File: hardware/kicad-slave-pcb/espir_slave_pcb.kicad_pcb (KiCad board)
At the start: 2 copper layers, 53.5 x 47 mm, 38 parts, among them Q2 AO3400A, Q4 AO3401A, SW1 RESET, SW2 BOOT, SW3 SS12D07VG6, U2 IR333C, U3 IR333C, U5 ESP32-C6-MINI-1, U6 AP2112K-3.3, U7 LiPo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

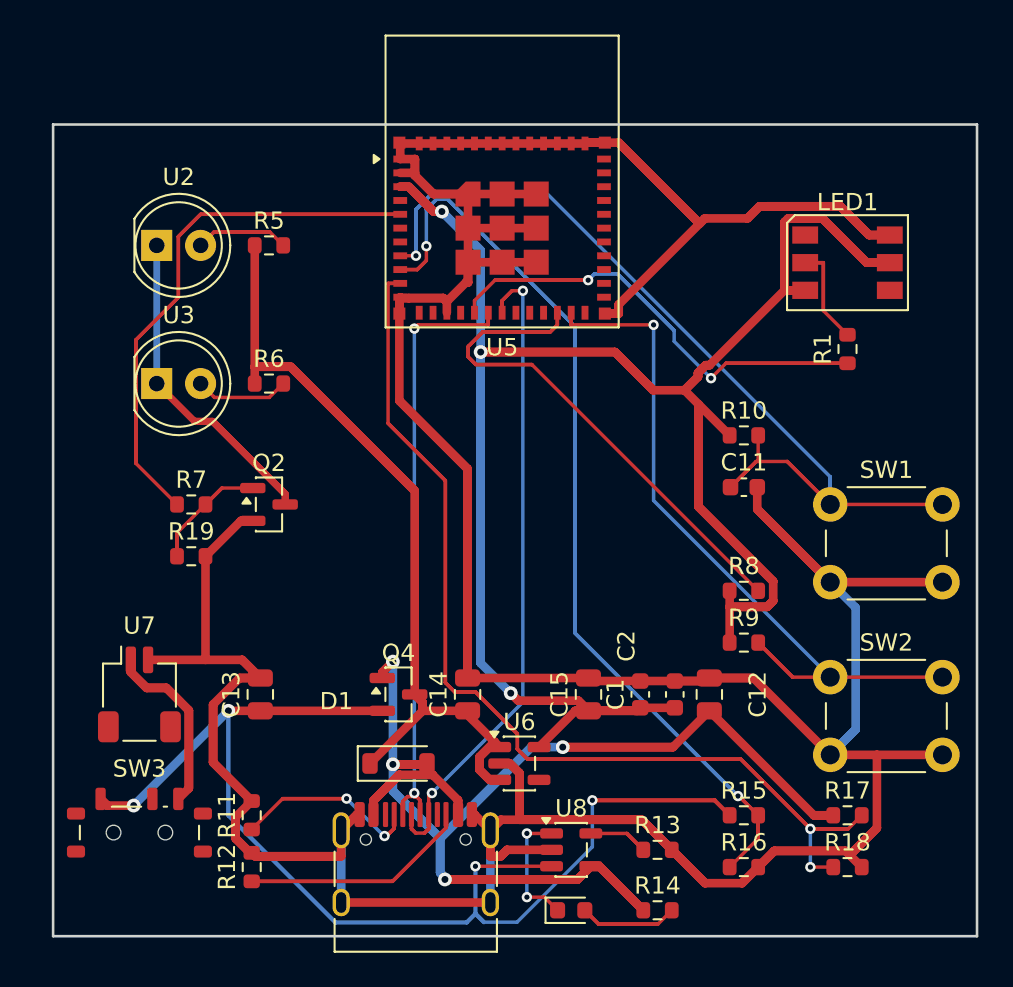
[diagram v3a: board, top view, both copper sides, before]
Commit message: hardware: convert slave PCB to 4-layer, wide VBAT, GND planes
Per request — minimal cost delta, don't sacrifice stability:
- 4 copper layers (F/In1/In2/B) via place_and_outline; GND pours on all four
  layers + collision-checked stitching-via grid (pour_gnd.py) → inner ground
  reference planes.
- The extra routing room lets every Power-class rail, including VBAT, route at
  0.5 mm (dropped the 2-layer VBAT 0.2 mm compromise; .kicad_dru back to 0.5).
- Fully routed 114/114 (310 tracks, 43 vias). LDO EN (tied to VSYS, boxed by
  U6's VIN/GND pins) jumpered VIN→EN on B.Cu under the GND pin.
- Grew board to 54 mm wide so the edge buttons clear the edge without colliding
  with the strap resistors; re-centred on A4.
- Silkscreen: collision-aware designator placement (fix_silk.py), hide refs with
  no clear spot.

DRC: 0 electrical violations (0 unconnected/track-width/clearance/edge/shorts).
Remaining 4 silk_edge_clearance (antenna/USB-C outlines overhang edges, by design)
+ 1 lib_footprint_mismatch (U5 vs latest library, same 61 pads, benign).
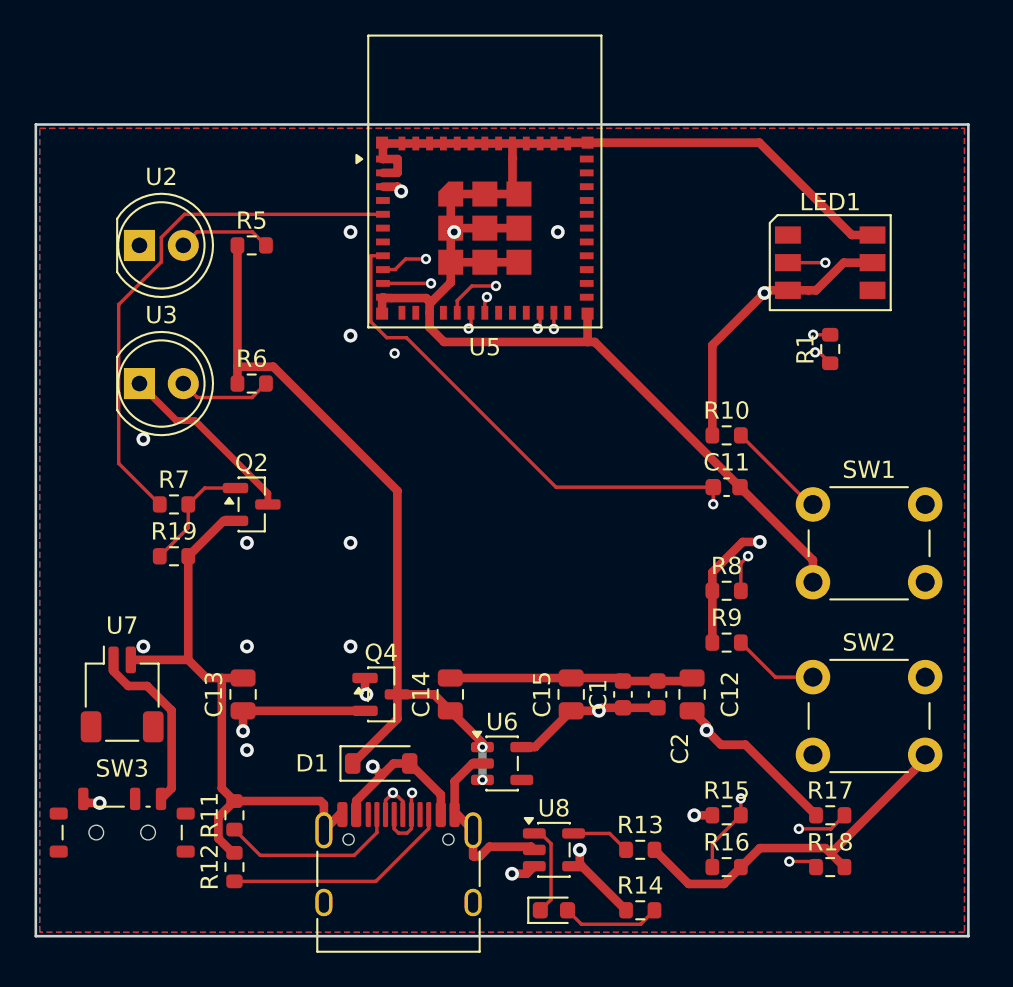
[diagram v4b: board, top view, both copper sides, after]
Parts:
- moved C1 1.00 mm to (155.5, 114.5)
- moved C11 1.00 mm to (161.5, 102.5)
- moved C12 1.00 mm to (159.5, 114.5)
- moved C13 1.00 mm to (133.5, 114.5)
- moved C14 1.00 mm to (145.5, 114.5)
- moved C15 1.00 mm to (152.5, 114.5)
- moved C2 1.00 mm to (157.5, 114.5)
- moved D1 1.00 mm to (141.5, 118.5)
- moved LED1 1.00 mm to (167.5, 89.5)
- moved LED2 1.00 mm to (151.5, 127.0)
- moved Q2 1.00 mm to (134.0, 103.5)
- moved Q4 1.00 mm to (141.5, 114.5)
- moved R1 1.00 mm to (167.5, 94.5)
- moved R10 1.00 mm to (161.5, 99.5)
- moved R11 1.00 mm to (133.0, 121.5)
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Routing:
- net GND: track 351.8 -> 203.6 mm, vias 0 -> 11
- net V3V3: track 171.0 -> 86.2 mm, vias 3 -> 4
- net BATT_SENSE: track 100.6 -> 46.2 mm
- net V5: track 106.3 -> 53.7 mm
- net VBUS_SENSE: track 101.6 -> 51.6 mm, vias 2 -> 3
- net IR1: track 58.4 -> 30.9 mm
- net EN: track 69.7 -> 47.4 mm
- net WS_GPIO: track 45.1 -> 24.5 mm
- net STRAP8: track 40.2 -> 22.9 mm, vias 0 -> 2
- net VSYS: track 62.5 -> 45.3 mm, vias 0 -> 2
- net VBAT: track 69.4 -> 52.8 mm
- net N$2: track 25.8 -> 13.3 mm
- net VCELL: track 19.9 -> 10.3 mm
- net IRD: track 26.3 -> 18.7 mm
- net BOOT: track 45.1 -> 38.9 mm
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- added copper zone on B.Cu, net GND
- added copper zone on F.Cu, net GND
- added copper zone on In1.Cu, net GND
- added copper zone on In2.Cu, net GND
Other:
- board size 53.5 x 47 mm -> 54 x 47 mm
- copper layers 2 -> 4

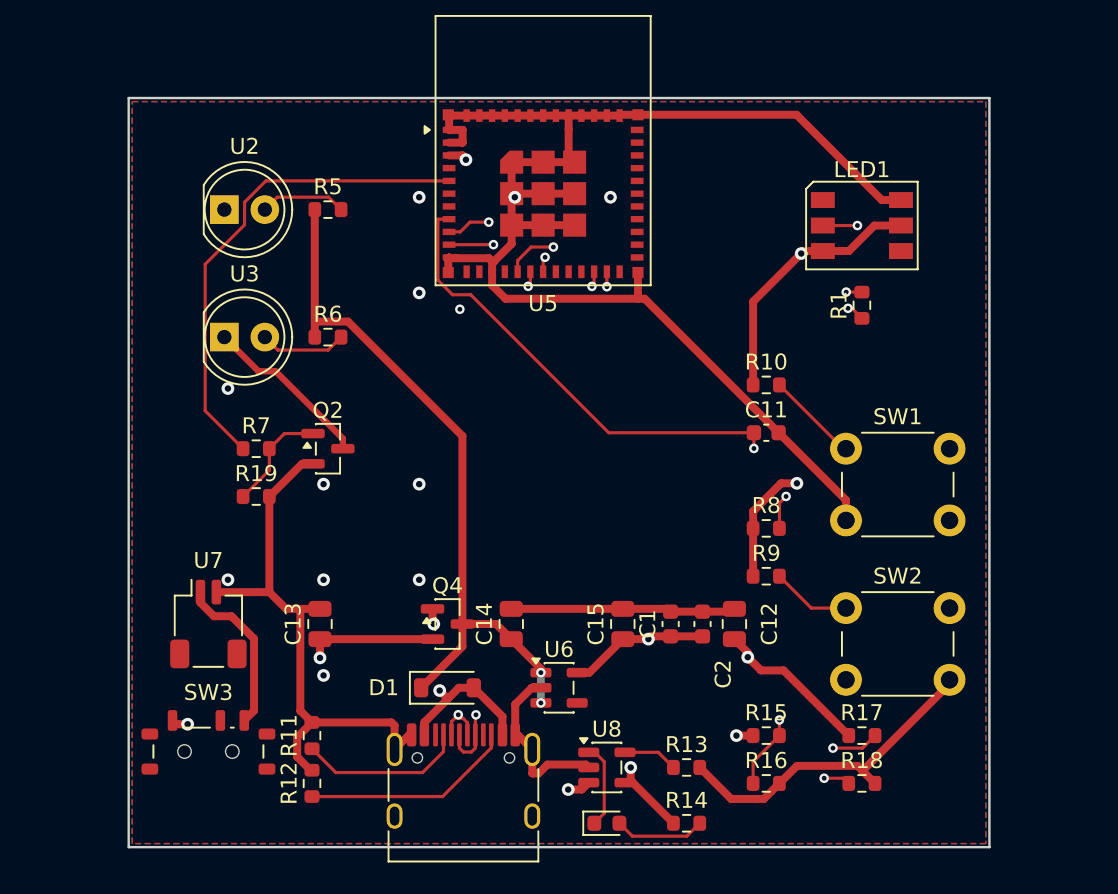
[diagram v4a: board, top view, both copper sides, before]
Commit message: hardware: round corners + 4x M3 mounting holes (expand board on X)
mounting_and_round.py (runs on the routed board — no re-route needed):
- expand the board on X to 66mm (symmetric, stays centred) so the packed
  components get clear left/right margins;
- round all four corners (r=3mm);
- add 4x M3 mounting holes (3.2mm Edge.Cuts cutouts) in the new margins, clear
  of every component — the GND pour isolates them with a ring.

pour_gnd.py: re-pour to the new outline; do all collection reads (tracks, pads)
before any writes (a SetLocalZoneConnection mid-iteration corrupts SWIG so a
later GetTracks returns a raw object); use SHAPE_LINE_CHAIN+AddPolygon for the
zone outline; treat existing vias as stitching obstacles (no hole_to_hole).

DRC: 0 unconnected, 0 electrical violations; 4 benign silk_edge + 1 benign
lib_footprint_mismatch.
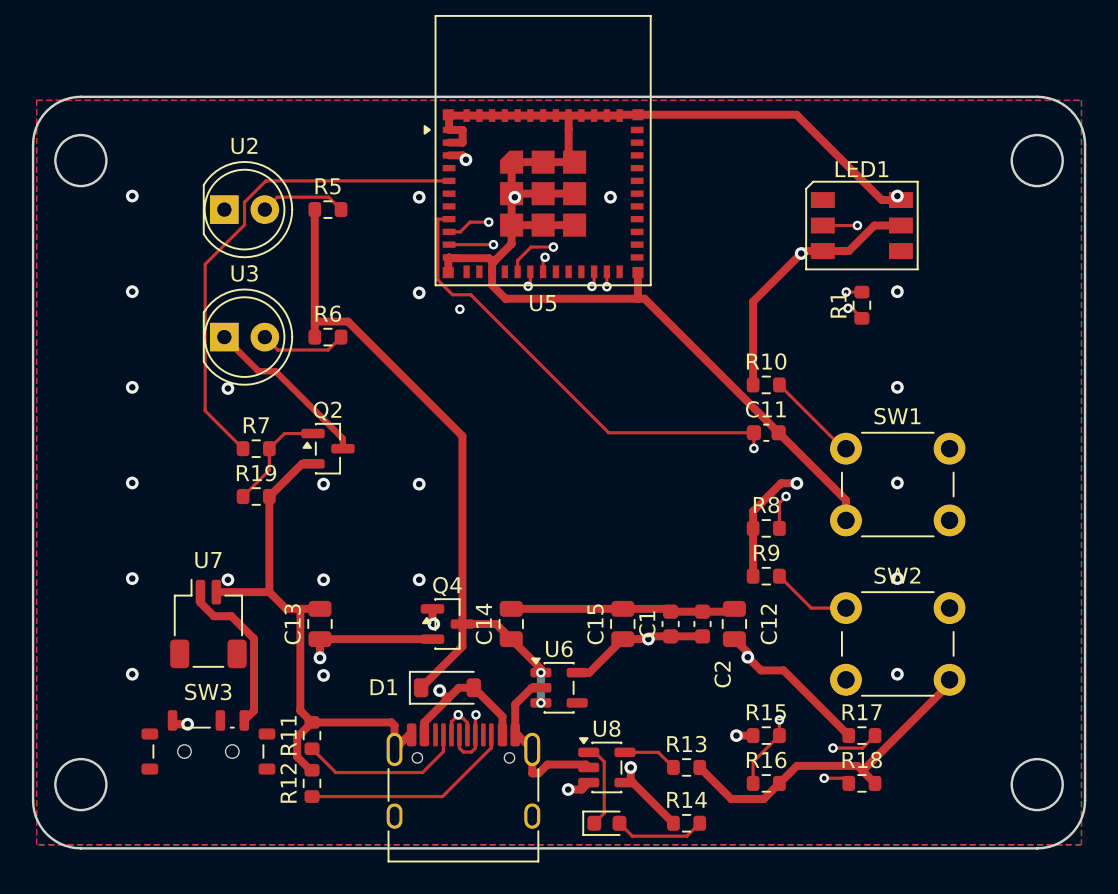
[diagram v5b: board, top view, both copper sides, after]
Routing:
- net GND: vias 11 -> 23
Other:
- board size 54 x 47 mm -> 66 x 47.1 mm

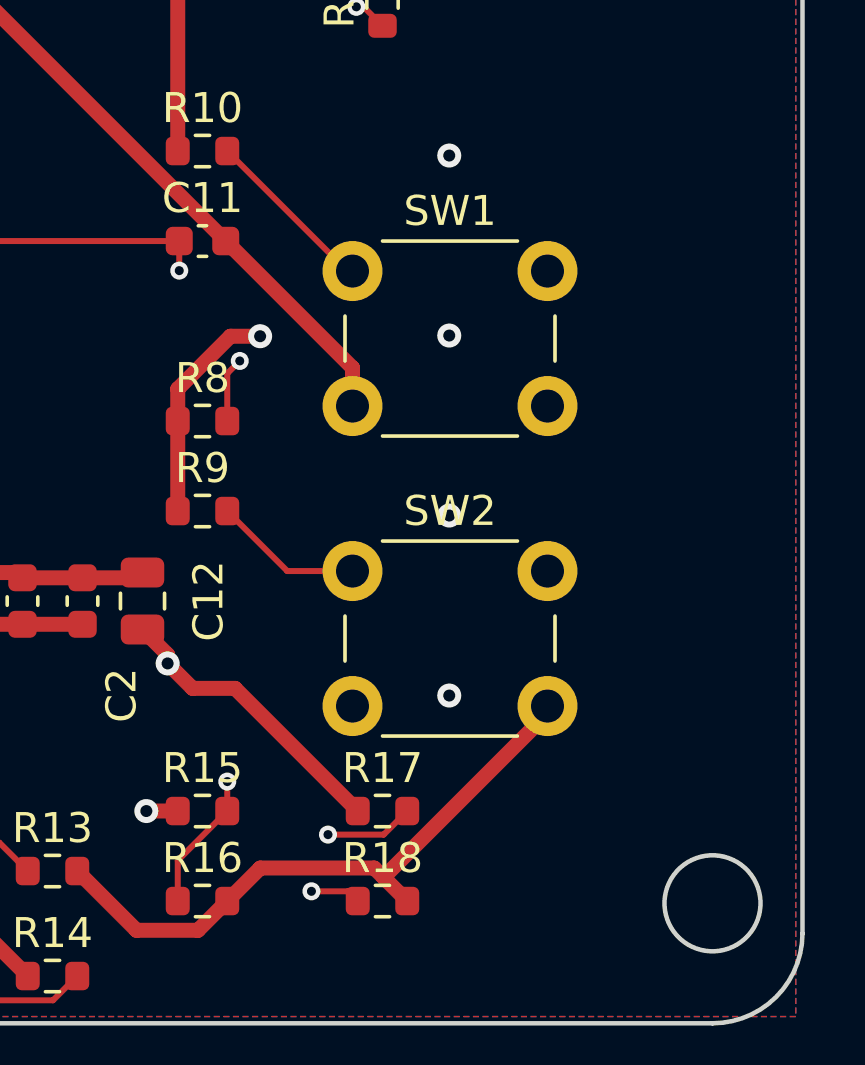
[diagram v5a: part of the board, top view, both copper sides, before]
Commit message: hardware: change RESET/BOOT buttons from THT 6mm to SMD tactile (KMR2)
Swap SW1/SW2 from Button_Switch_THT:SW_PUSH_6mm to
Button_Switch_SMD:SW_Push_1P1T_NO_CK_KMR2, in both the SKiDL source and the
routed board (swap_smd_button.py, run per-button in its own process to dodge
pcbnew SWIG state corruption):
- assign the new pads' nets AFTER Add (Add clears nets set beforehand);
- bridge the EN/BOOT signal once per old pad position to the nearest new pad;
- add a via at each old (through-hole) pad position so the inner/bottom-layer
  tracks that connected through the THT hole stay on-net;
- drop the dangling GND stubs — the 4-layer GND pour reconnects the new GND pads.

DRC: 0 unconnected, 0 electrical violations (only the 4 benign edge-silk + 1
benign lib_footprint_mismatch). 3D-verified the two SMD buttons.
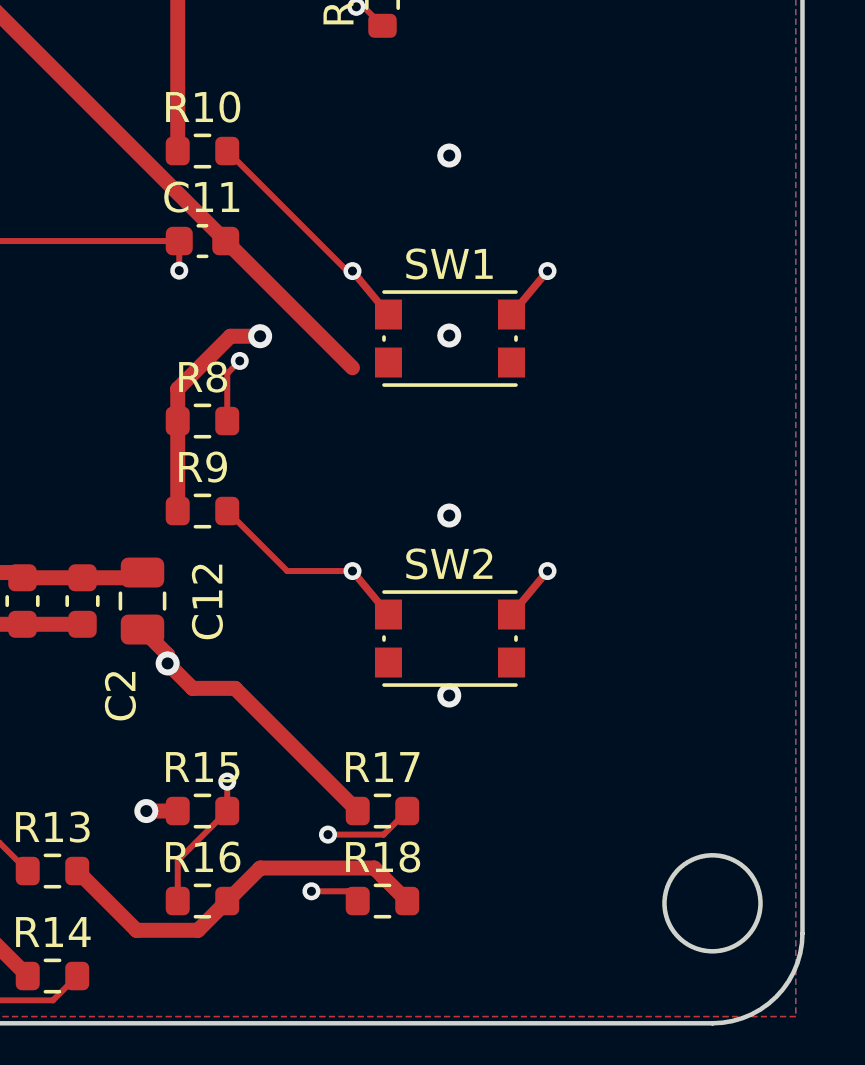
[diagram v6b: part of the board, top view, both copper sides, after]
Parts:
- SW1, SW2: footprint Button_Switch_THT:SW_PUSH_6mm -> SW_Push_1P1T_NO_CK_KMR2
- moved SW1 3.95 mm to (169.8, 105.8)
- moved SW2 3.95 mm to (169.8, 115.8)
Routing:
- net GND: track 203.6 -> 181.4 mm
- net EN: track 47.4 -> 51.2 mm, vias 1 -> 3
- net BOOT: track 38.9 -> 42.7 mm, vias 1 -> 3

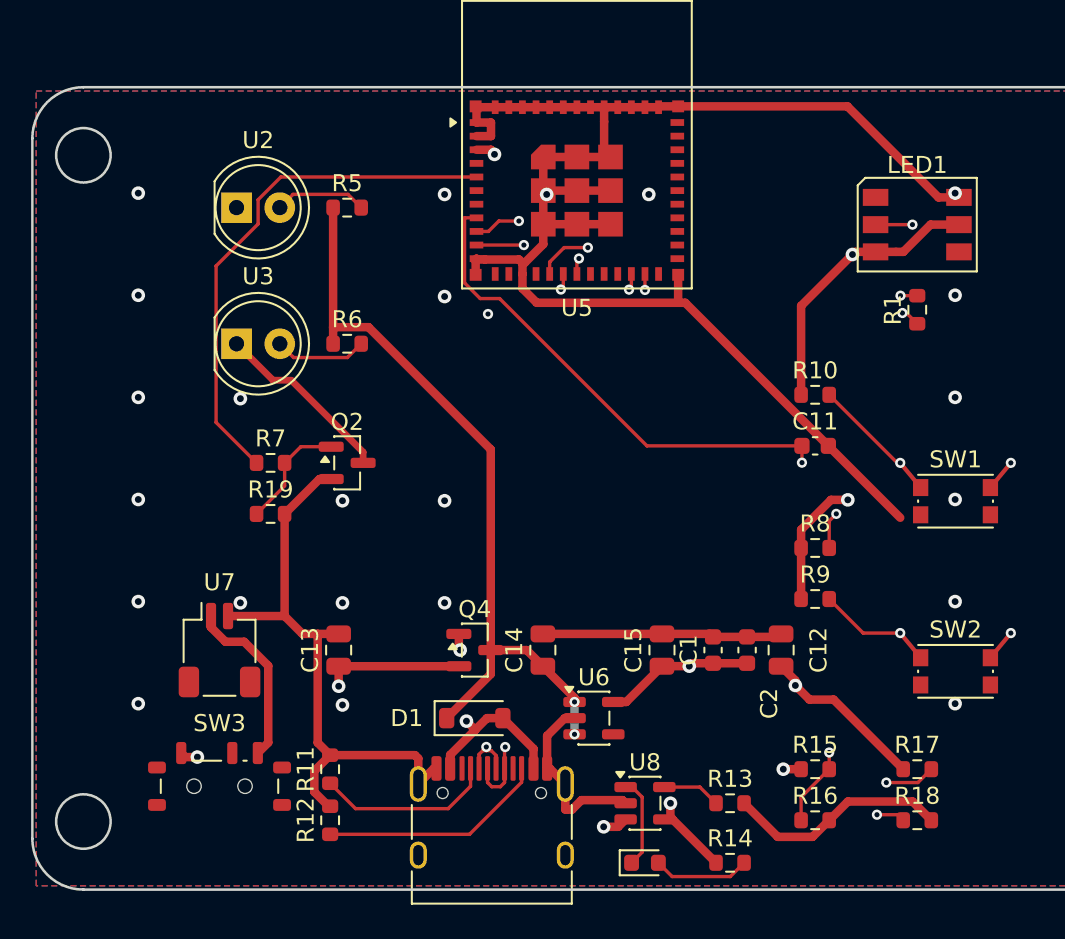
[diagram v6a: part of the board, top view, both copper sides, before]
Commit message: hardware: re-solve routing after U7 (JST battery connector) move
U7 was moved + rotated -90° in the GUI, which broke local routing:
- VCELL (U7.1 -> SW3.3) left dangling in two pieces -> cleared the fragments
  and re-routed it on F.Cu (right, then down, clear of U7's own GND pad), 0.5mm
  Power class;
- U7's mounting pads landed on two GND stitch vias (short + hole-clearance +
  mask-bridge) -> removed those two vias (the pour still grounds the area);
- trimmed a stray dangling V3V3 stub.
Re-poured all four GND layers.

DRC: 0 unconnected, 0 electrical violations (only the 4 benign edge-silk + 1
benign lib_footprint_mismatch).
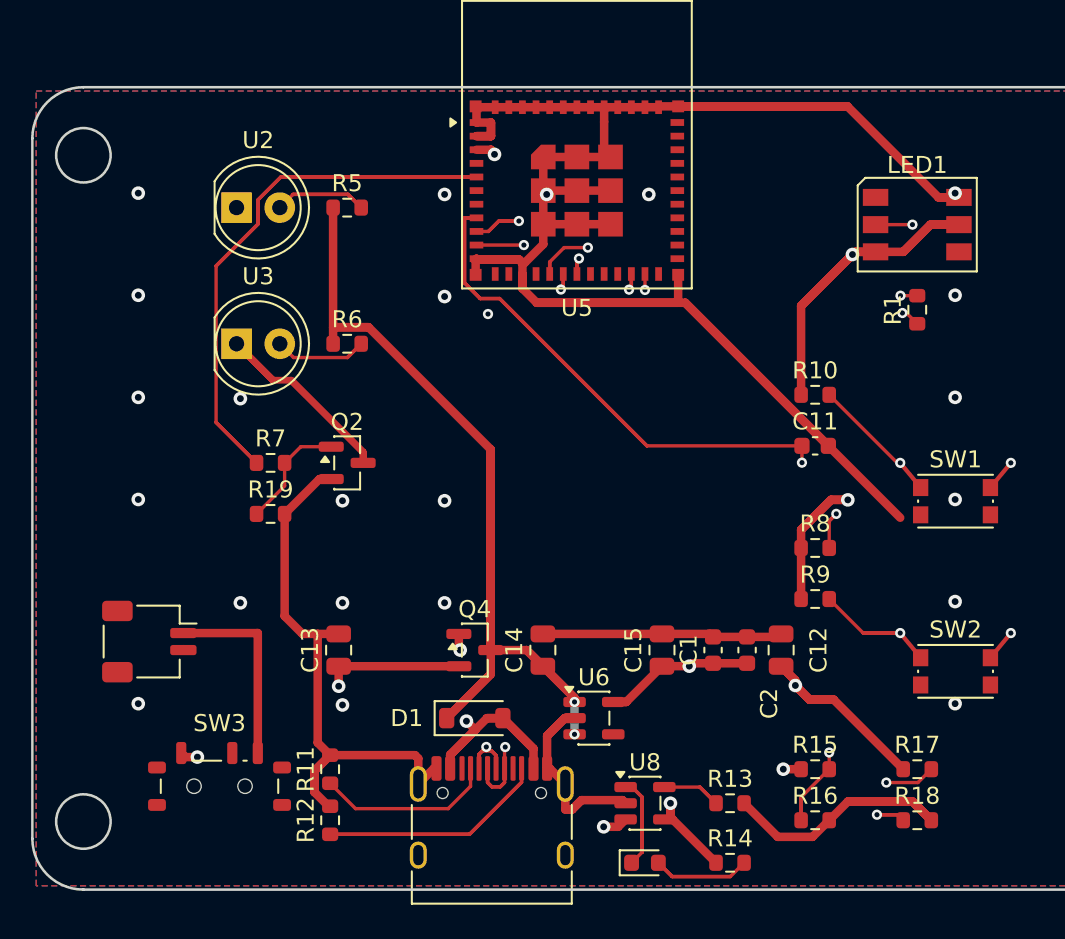
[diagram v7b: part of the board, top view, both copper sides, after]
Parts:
- moved U7 4.16 mm to (122.4, 114.0), turned to -90 degrees
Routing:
- net GND: track 181.4 -> 226.1 mm, vias 23 -> 22
- net USB_DP: track 41.8 -> 77.4 mm
- net VBUS_SENSE: track 51.6 -> 83.5 mm
- net V3V3: track 86.2 -> 117.5 mm
- net IR1: track 30.9 -> 52.5 mm
- net VSYS: track 45.3 -> 66.8 mm
- net STRAP8: track 22.9 -> 44.0 mm
- net EN: track 51.2 -> 70.6 mm
- net WS_GPIO: track 24.5 -> 40.1 mm
- net V5: track 53.7 -> 68.1 mm
- net N$2: track 13.3 -> 25.8 mm
- net VBAT: track 52.8 -> 63.8 mm
- net IRD: track 18.7 -> 28.3 mm
- net STAT: track 5.33 -> 13.4 mm
- net BOOT: track 42.7 -> 47.6 mm
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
